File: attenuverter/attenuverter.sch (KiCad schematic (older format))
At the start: 28 parts, among them J1 Conn_01x03_Male, J2 Conn_01x02_Male, J3 Conn_01x02_Male, J4 Conn_01x02_Male, J5 Conn_01x02_Male, J6 Conn_01x02_Male, J7 Conn_01x02_Male, J8 Conn_01x02_Male, J9 Conn_01x02_Male, U1 TL074

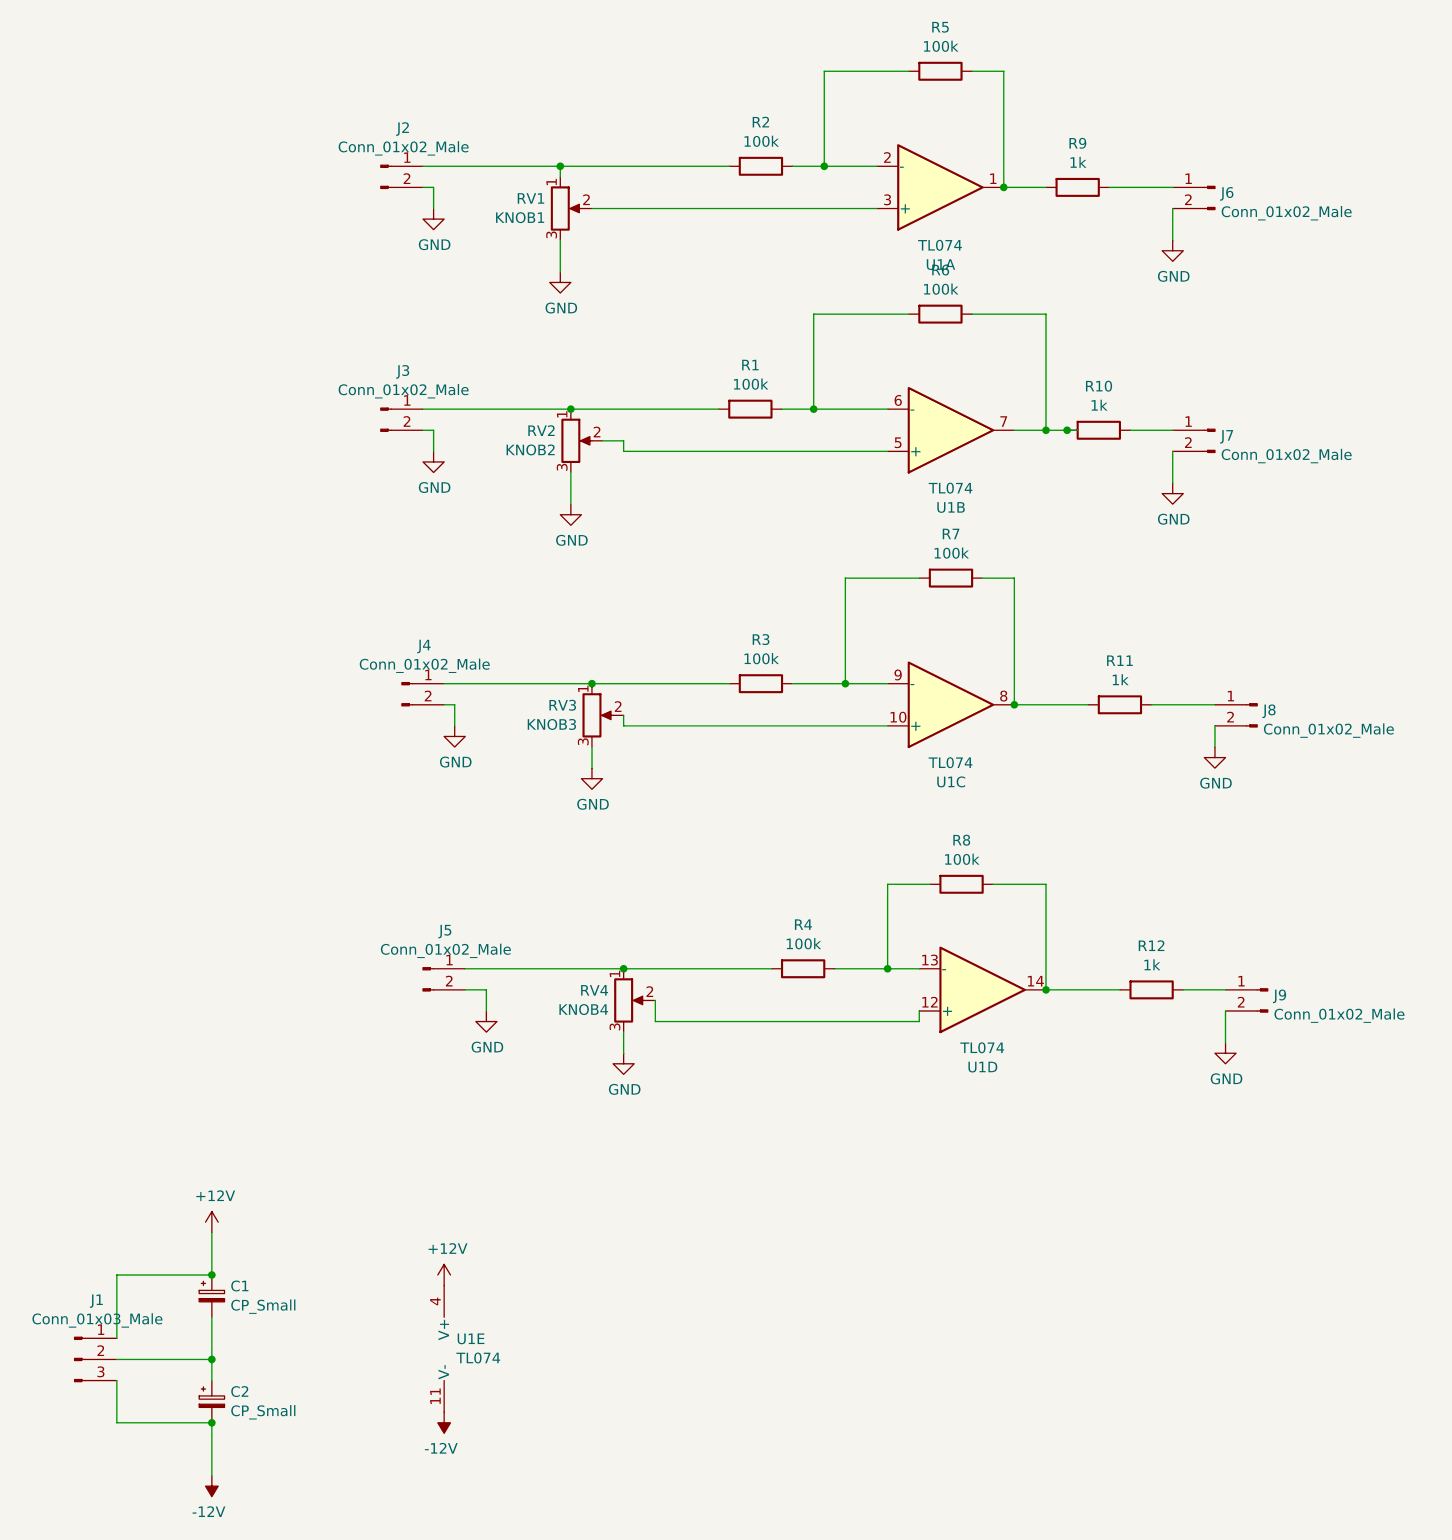
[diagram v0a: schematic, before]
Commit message: three new modules with pcbs
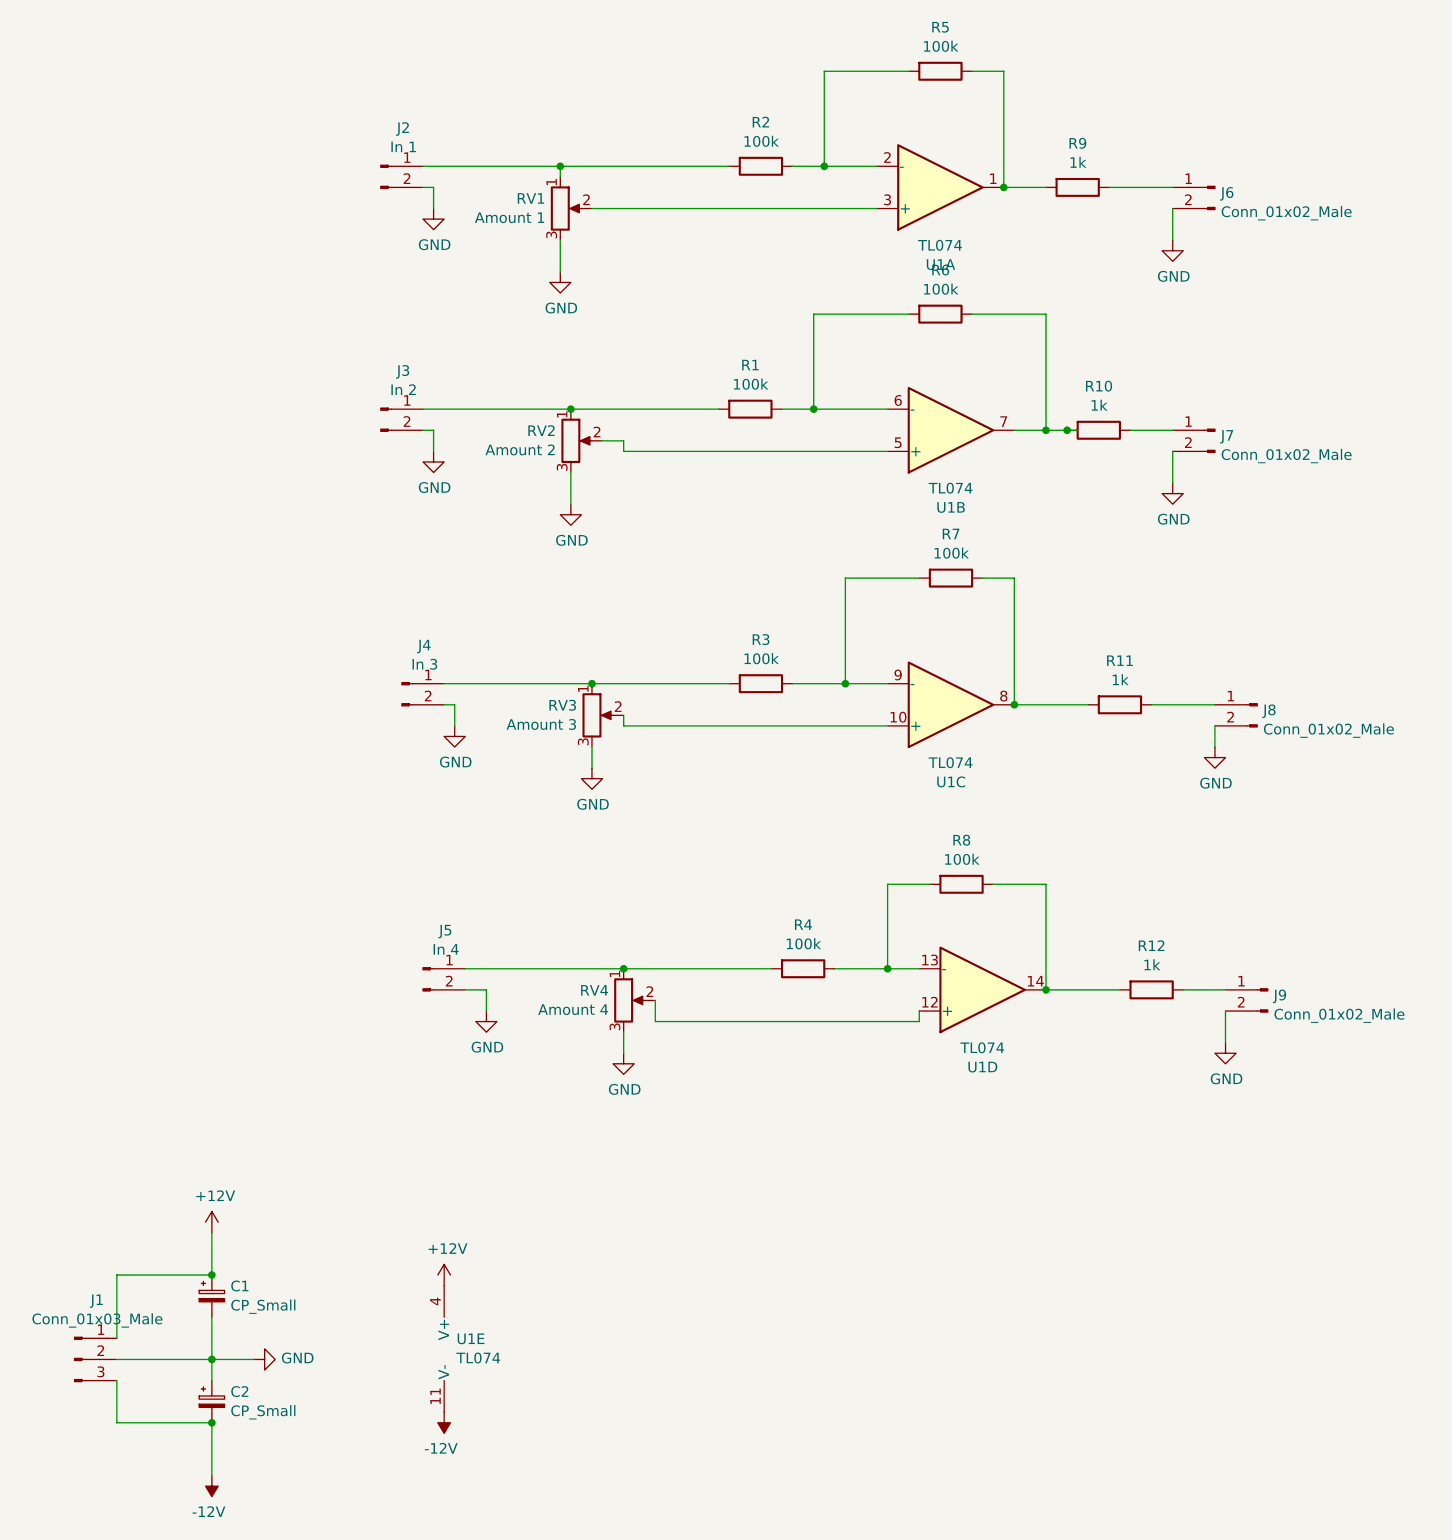
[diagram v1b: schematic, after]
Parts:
- C1, C2: footprint (none) -> Capacitor_THT:CP_Radial_Tantal_D5.0mm_P2.50mm
- J1: footprint (none) -> Connector_PinHeader_2.54mm:PinHeader_1x03_P2.54mm_Vertical
- J2: value Conn_01x02_Male -> In 1; footprint (none) -> Connector_PinHeader_2.54mm:PinHeader_1x02_P2.54mm_Vertical
- J3: value Conn_01x02_Male -> In 2; footprint (none) -> Connector_PinHeader_2.54mm:PinHeader_1x02_P2.54mm_Vertical
- J4: value Conn_01x02_Male -> In 3; footprint (none) -> Connector_PinHeader_2.54mm:PinHeader_1x02_P2.54mm_Vertical
- J5: value Conn_01x02_Male -> In 4; footprint (none) -> Connector_PinHeader_2.54mm:PinHeader_1x02_P2.54mm_Vertical
- J6, J7, J8, J9: footprint (none) -> Connector_PinHeader_2.54mm:PinHeader_1x02_P2.54mm_Vertical
- R1, R10, R11, R12, R2, R3, R4, R5, R6, R7, R8, R9: footprint (none) -> Resistor_THT:R_Axial_DIN0207_L6.3mm_D2.5mm_P7.62mm_Horizontal
- RV1: value KNOB1 -> Amount 1; footprint (none) -> Connector_PinHeader_2.54mm:PinHeader_1x03_P2.54mm_Vertical
- RV2: value KNOB2 -> Amount 2; footprint (none) -> Connector_PinHeader_2.54mm:PinHeader_1x03_P2.54mm_Vertical
- RV3: value KNOB3 -> Amount 3; footprint (none) -> Connector_PinHeader_2.54mm:PinHeader_1x03_P2.54mm_Vertical
- RV4: value KNOB4 -> Amount 4; footprint (none) -> Connector_PinHeader_2.54mm:PinHeader_1x03_P2.54mm_Vertical
- U1: footprint (none) -> Package_DIP:DIP-14_W7.62mm_Socket
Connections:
- net GND: now also C1.2, C2.1, J1.2 (Pin_2)
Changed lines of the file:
@@
 F 0 "U1" H 5400 1767 50  0000 C CNN
 F 1 "TL074" H 5400 1676 50  0000 C CNN
-F 2 "" H 5350 1500 50  0001 C CNN
+F 2 "Package_DIP:DIP-14_W7.62mm_Socket" H 5350 1500 50  0001 C CNN
 F 3 "http://www.ti.com/lit/ds/symlink/tl071.pdf" H 5450 1600 50  0001 C CNN
 	1    5400 1400
@@
 F 0 "U1" H 5450 2917 50  0000 C CNN
 F 1 "TL074" H 5450 2826 50  0000 C CNN
-F 2 "" H 5400 2650 50  0001 C CNN
+F 2 "Package_DIP:DIP-14_W7.62mm_Socket" H 5400 2650 50  0001 C CNN
 F 3 "http://www.ti.com/lit/ds/symlink/tl071.pdf" H 5500 2750 50  0001 C CNN
 	2    5450 2550
@@
 F 0 "U1" H 5450 4217 50  0000 C CNN
 F 1 "TL074" H 5450 4126 50  0000 C CNN
-F 2 "" H 5400 3950 50  0001 C CNN
+F 2 "Package_DIP:DIP-14_W7.62mm_Socket" H 5400 3950 50  0001 C CNN
 F 3 "http://www.ti.com/lit/ds/symlink/tl071.pdf" H 5500 4050 50  0001 C CNN
 	3    5450 3850
@@
 F 0 "U1" H 5600 5567 50  0000 C CNN
 F 1 "TL074" H 5600 5476 50  0000 C CNN
-F 2 "" H 5550 5300 50  0001 C CNN
+F 2 "Package_DIP:DIP-14_W7.62mm_Socket" H 5550 5300 50  0001 C CNN
 F 3 "http://www.ti.com/lit/ds/symlink/tl071.pdf" H 5650 5400 50  0001 C CNN
 	4    5600 5200
@@
 F 0 "R5" V 5193 850 50  0000 C CNN
 F 1 "100k" V 5284 850 50  0000 C CNN
-F 2 "" V 5330 850 50  0001 C CNN
+F 2 "Resistor_THT:R_Axial_DIN0207_L6.3mm_D2.5mm_P7.62mm_Horizontal" V 5330 850 50  0001 C CNN
 F 3 "~" H 5400 850 50  0001 C CNN
 	1    5400 850
@@
 F 0 "R2" V 4343 1300 50  0000 C CNN
 F 1 "100k" V 4434 1300 50  0000 C CNN
-F 2 "" V 4480 1300 50  0001 C CNN
+F 2 "Resistor_THT:R_Axial_DIN0207_L6.3mm_D2.5mm_P7.62mm_Horizontal" V 4480 1300 50  0001 C CNN
 F 3 "~" H 4550 1300 50  0001 C CNN
 	1    4550 1300
@@
 F 0 "R6" V 5193 2000 50  0000 C CNN
 F 1 "100k" V 5284 2000 50  0000 C CNN
-F 2 "" V 5330 2000 50  0001 C CNN
+F 2 "Resistor_THT:R_Axial_DIN0207_L6.3mm_D2.5mm_P7.62mm_Horizontal" V 5330 2000 50  0001 C CNN
 F 3 "~" H 5400 2000 50  0001 C CNN
 	1    5400 2000
@@
 F 0 "R1" V 4293 2450 50  0000 C CNN
 F 1 "100k" V 4384 2450 50  0000 C CNN
-F 2 "" V 4430 2450 50  0001 C CNN
+F 2 "Resistor_THT:R_Axial_DIN0207_L6.3mm_D2.5mm_P7.62mm_Horizontal" V 4430 2450 50  0001 C CNN
 F 3 "~" H 4500 2450 50  0001 C CNN
 	1    4500 2450
@@
 F 0 "R7" V 5243 3250 50  0000 C CNN
 F 1 "100k" V 5334 3250 50  0000 C CNN
-F 2 "" V 5380 3250 50  0001 C CNN
+F 2 "Resistor_THT:R_Axial_DIN0207_L6.3mm_D2.5mm_P7.62mm_Horizontal" V 5380 3250 50  0001 C CNN
 F 3 "~" H 5450 3250 50  0001 C CNN
 	1    5450 3250
@@
 F 0 "R3" V 4343 3750 50  0000 C CNN
 F 1 "100k" V 4434 3750 50  0000 C CNN
-F 2 "" V 4480 3750 50  0001 C CNN
+F 2 "Resistor_THT:R_Axial_DIN0207_L6.3mm_D2.5mm_P7.62mm_Horizontal" V 4480 3750 50  0001 C CNN
 F 3 "~" H 4550 3750 50  0001 C CNN
 	1    4550 3750
@@
 F 0 "R8" V 5293 4700 50  0000 C CNN
 F 1 "100k" V 5384 4700 50  0000 C CNN
-F 2 "" V 5430 4700 50  0001 C CNN
+F 2 "Resistor_THT:R_Axial_DIN0207_L6.3mm_D2.5mm_P7.62mm_Horizontal" V 5430 4700 50  0001 C CNN
 F 3 "~" H 5500 4700 50  0001 C CNN
 	1    5500 4700
@@
 F 0 "R4" V 4543 5100 50  0000 C CNN
 F 1 "100k" V 4634 5100 50  0000 C CNN
-F 2 "" V 4680 5100 50  0001 C CNN
+F 2 "Resistor_THT:R_Axial_DIN0207_L6.3mm_D2.5mm_P7.62mm_Horizontal" V 4680 5100 50  0001 C CNN
 F 3 "~" H 4750 5100 50  0001 C CNN
 	1    4750 5100
@@
 F 0 "R12" V 6193 5200 50  0000 C CNN
 F 1 "1k" V 6284 5200 50  0000 C CNN
-F 2 "" V 6330 5200 50  0001 C CNN
+F 2 "Resistor_THT:R_Axial_DIN0207_L6.3mm_D2.5mm_P7.62mm_Horizontal" V 6330 5200 50  0001 C CNN
 F 3 "~" H 6400 5200 50  0001 C CNN
 	1    6400 5200
@@
 F 0 "R11" V 6043 3850 50  0000 C CNN
 F 1 "1k" V 6134 3850 50  0000 C CNN
-F 2 "" V 6180 3850 50  0001 C CNN
+F 2 "Resistor_THT:R_Axial_DIN0207_L6.3mm_D2.5mm_P7.62mm_Horizontal" V 6180 3850 50  0001 C CNN
 F 3 "~" H 6250 3850 50  0001 C CNN
 	1    6250 3850
@@
 F 0 "R10" V 5943 2550 50  0000 C CNN
 F 1 "1k" V 6034 2550 50  0000 C CNN
-F 2 "" V 6080 2550 50  0001 C CNN
+F 2 "Resistor_THT:R_Axial_DIN0207_L6.3mm_D2.5mm_P7.62mm_Horizontal" V 6080 2550 50  0001 C CNN
 F 3 "~" H 6150 2550 50  0001 C CNN
 	1    6150 2550
@@
 F 0 "R9" V 5843 1400 50  0000 C CNN
 F 1 "1k" V 5934 1400 50  0000 C CNN
-F 2 "" V 5980 1400 50  0001 C CNN
+F 2 "Resistor_THT:R_Axial_DIN0207_L6.3mm_D2.5mm_P7.62mm_Horizontal" V 5980 1400 50  0001 C CNN
 F 3 "~" H 6050 1400 50  0001 C CNN
 	1    6050 1400
@@
 P 2750 1300
 F 0 "J2" H 2858 1481 50  0000 C CNN
-F 1 "Conn_01x02_Male" H 2858 1390 50  0000 C CNN
-F 2 "" H 2750 1300 50  0001 C CNN
+F 1 "In 1" H 2858 1390 50  0000 C CNN
+F 2 "Connector_PinHeader_2.54mm:PinHeader_1x02_P2.54mm_Vertical" H 2750 1300 50  0001 C CNN
 F 3 "~" H 2750 1300 50  0001 C CNN
 	1    2750 1300
@@
 P 2750 2450
 F 0 "J3" H 2858 2631 50  0000 C CNN
-F 1 "Conn_01x02_Male" H 2858 2540 50  0000 C CNN
-F 2 "" H 2750 2450 50  0001 C CNN
+F 1 "In 2" H 2858 2540 50  0000 C CNN
+F 2 "Connector_PinHeader_2.54mm:PinHeader_1x02_P2.54mm_Vertical" H 2750 2450 50  0001 C CNN
 F 3 "~" H 2750 2450 50  0001 C CNN
 	1    2750 2450
@@
 P 2850 3750
 F 0 "J4" H 2958 3931 50  0000 C CNN
-F 1 "Conn_01x02_Male" H 2958 3840 50  0000 C CNN
-F 2 "" H 2850 3750 50  0001 C CNN
+F 1 "In 3" H 2958 3840 50  0000 C CNN
+F 2 "Connector_PinHeader_2.54mm:PinHeader_1x02_P2.54mm_Vertical" H 2850 3750 50  0001 C CNN
 F 3 "~" H 2850 3750 50  0001 C CNN
 	1    2850 3750
@@
 P 2950 5100
 F 0 "J5" H 3058 5281 50  0000 C CNN
-F 1 "Conn_01x02_Male" H 3058 5190 50  0000 C CNN
-F 2 "" H 2950 5100 50  0001 C CNN
+F 1 "In 4" H 3058 5190 50  0000 C CNN
+F 2 "Connector_PinHeader_2.54mm:PinHeader_1x02_P2.54mm_Vertical" H 2950 5100 50  0001 C CNN
 F 3 "~" H 2950 5100 50  0001 C CNN
 	1    2950 5100
@@
 P 3600 1500
 F 0 "RV1" H 3530 1546 50  0000 R CNN
-F 1 "KNOB1" H 3530 1455 50  0000 R CNN
-F 2 "" H 3600 1500 50  0001 C CNN
+F 1 "Amount 1" H 3530 1455 50  0000 R CNN
+F 2 "Connector_PinHeader_2.54mm:PinHeader_1x03_P2.54mm_Vertical" H 3600 1500 50  0001 C CNN
 F 3 "~" H 3600 1500 50  0001 C CNN
 	1    3600 1500
@@
 P 3650 2600
 F 0 "RV2" H 3580 2646 50  0000 R CNN
-F 1 "KNOB2" H 3580 2555 50  0000 R CNN
-F 2 "" H 3650 2600 50  0001 C CNN
+F 1 "Amount 2" H 3580 2555 50  0000 R CNN
+F 2 "Connector_PinHeader_2.54mm:PinHeader_1x03_P2.54mm_Vertical" H 3650 2600 50  0001 C CNN
 F 3 "~" H 3650 2600 50  0001 C CNN
 	1    3650 2600
@@
 P 3750 3900
 F 0 "RV3" H 3680 3946 50  0000 R CNN
-F 1 "KNOB3" H 3680 3855 50  0000 R CNN
-F 2 "" H 3750 3900 50  0001 C CNN
+F 1 "Amount 3" H 3680 3855 50  0000 R CNN
+F 2 "Connector_PinHeader_2.54mm:PinHeader_1x03_P2.54mm_Vertical" H 3750 3900 50  0001 C CNN
 F 3 "~" H 3750 3900 50  0001 C CNN
 	1    3750 3900
@@
 P 3900 5250
 F 0 "RV4" H 3830 5296 50  0000 R CNN
-F 1 "KNOB4" H 3830 5205 50  0000 R CNN
-F 2 "" H 3900 5250 50  0001 C CNN
+F 1 "Amount 4" H 3830 5205 50  0000 R CNN
+F 2 "Connector_PinHeader_2.54mm:PinHeader_1x03_P2.54mm_Vertical" H 3900 5250 50  0001 C CNN
 F 3 "~" H 3900 5250 50  0001 C CNN
 	1    3900 5250
@@
 F 0 "J6" H 6672 1374 50  0000 R CNN
 F 1 "Conn_01x02_Male" H 6672 1283 50  0000 R CNN
-F 2 "" H 6700 1400 50  0001 C CNN
+F 2 "Connector_PinHeader_2.54mm:PinHeader_1x02_P2.54mm_Vertical" H 6700 1400 50  0001 C CNN
 F 3 "~" H 6700 1400 50  0001 C CNN
 	1    6700 1400
@@
 F 0 "J7" H 6672 2524 50  0000 R CNN
 F 1 "Conn_01x02_Male" H 6672 2433 50  0000 R CNN
-F 2 "" H 6700 2550 50  0001 C CNN
+F 2 "Connector_PinHeader_2.54mm:PinHeader_1x02_P2.54mm_Vertical" H 6700 2550 50  0001 C CNN
 F 3 "~" H 6700 2550 50  0001 C CNN
 	1    6700 2550
@@
 F 0 "J8" H 6872 3824 50  0000 R CNN
 F 1 "Conn_01x02_Male" H 6872 3733 50  0000 R CNN
-F 2 "" H 6900 3850 50  0001 C CNN
+F 2 "Connector_PinHeader_2.54mm:PinHeader_1x02_P2.54mm_Vertical" H 6900 3850 50  0001 C CNN
 F 3 "~" H 6900 3850 50  0001 C CNN
 	1    6900 3850
@@
 F 0 "J9" H 6922 5174 50  0000 R CNN
 F 1 "Conn_01x02_Male" H 6922 5083 50  0000 R CNN
-F 2 "" H 6950 5200 50  0001 C CNN
+F 2 "Connector_PinHeader_2.54mm:PinHeader_1x02_P2.54mm_Vertical" H 6950 5200 50  0001 C CNN
 F 3 "~" H 6950 5200 50  0001 C CNN
 	1    6950 5200
@@
 F 0 "J1" H 1408 7231 50  0000 C CNN
 F 1 "Conn_01x03_Male" H 1408 7140 50  0000 C CNN
-F 2 "" H 1300 6950 50  0001 C CNN
+F 2 "Connector_PinHeader_2.54mm:PinHeader_1x03_P2.54mm_Vertical" H 1300 6950 50  0001 C CNN
 F 3 "~" H 1300 6950 50  0001 C CNN
 	1    1300 6950
@@
 F 0 "C1" H 2038 6696 50  0000 L CNN
 F 1 "CP_Small" H 2038 6605 50  0000 L CNN
-F 2 "" H 1950 6650 50  0001 C CNN
+F 2 "Capacitor_THT:CP_Radial_Tantal_D5.0mm_P2.50mm" H 1950 6650 50  0001 C CNN
 F 3 "~" H 1950 6650 50  0001 C CNN
 	1    1950 6650
@@
 F 0 "C2" H 2038 7196 50  0000 L CNN
 F 1 "CP_Small" H 2038 7105 50  0000 L CNN
-F 2 "" H 1950 7150 50  0001 C CNN
+F 2 "Capacitor_THT:CP_Radial_Tantal_D5.0mm_P2.50mm" H 1950 7150 50  0001 C CNN
 F 3 "~" H 1950 7150 50  0001 C CNN
 	1    1950 7150
@@
 F 0 "U1" H 3108 6946 50  0000 L CNN
 F 1 "TL074" H 3108 6855 50  0000 L CNN
-F 2 "" H 3100 7000 50  0001 C CNN
+F 2 "Package_DIP:DIP-14_W7.62mm_Socket" H 3100 7000 50  0001 C CNN
 F 3 "http://www.ti.com/lit/ds/symlink/tl071.pdf" H 3200 7100 50  0001 C CNN
 	5    3150 6900
@@
 Wire Wire Line
 	6750 5300 6750 5450
+$Comp
+L power:GND #PWR0101
+U 1 1 6003BE60
+P 2150 6950
+F 0 "#PWR0101" H 2150 6700 50  0001 C CNN
+F 1 "GND" V 2155 6822 50  0000 R CNN
+F 2 "" H 2150 6950 50  0001 C CNN
+F 3 "" H 2150 6950 50  0001 C CNN
+	1    2150 6950
+	0    -1   -1   0
+$EndComp
+Wire Wire Line
+	1950 6950 2150 6950
 $EndSCHEMATC
